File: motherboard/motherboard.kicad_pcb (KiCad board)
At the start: 2 copper layers, 33 parts, among them J1 Conn_01x02_Male, J2 Conn_01x02_Male, J3 Conn_01x02_Male, J4 Conn_01x02_Male, J5 XLR3, J6 Conn_01x02_Male, P1 Raspberry_Pi_+_Conn, Q1 Q_NMOS_GSD, Q2 Q_NMOS_GSD, U1 74AUC2G04, U2 4081, U3 TLC272, U4 TLC272

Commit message: First routing done!
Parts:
- removed C2: C, Capacitor_SMD:C_0603_1608Metric
- removed D4, D5: D, Diode_SMD:D_0603_1608Metric
- removed R12: 4.7k, Resistor_SMD:R_0201_0603Metric
- removed RV2: 10k, Potentiometer_SMD:Potentiometer_Vishay_TS53YL_Vertical
- removed U4: TLC272, Package_SO:TSSOP-8_4.4x3mm_P0.65mm
- added D1: d, Diode_SMD:D_0603_1608Metric, F.Cu at (115.4, 64.9)
- added G***: LOGO, silkscreen:logo_2, F.Cu at (103.1, 95.8)
- D2, D3: value d -> D
- J5: value XLR3 -> Conn_01x02_Male; footprint TerminalBlock_Phoenix:TerminalBlock_Phoenix_MKDS-3-3-5.08_1x03_P5.08mm_Horizontal -> TerminalBlock_Phoenix:TerminalBlock_Phoenix_MKDS-1,5-2-5.08_1x02_P5.08mm_Horizontal
- J6: value Conn_01x02_Male -> XLR3; footprint TerminalBlock_Phoenix:TerminalBlock_Phoenix_MKDS-1,5-2-5.08_1x02_P5.08mm_Horizontal -> TerminalBlock_Phoenix:TerminalBlock_Phoenix_MKDS-3-3-5.08_1x03_P5.08mm_Horizontal
- R1, R10, R2, R3, R8: footprint Resistor_SMD:R_0201_0603Metric -> Resistor_SMD:R_0603_1608Metric_Pad1.05x0.95mm_HandSolder
- R11: value 100 -> 4.7k; footprint Resistor_SMD:R_0201_0603Metric -> Resistor_SMD:R_0603_1608Metric_Pad1.05x0.95mm_HandSolder
- R4: value 230 -> 100k; footprint Resistor_SMD:R_0201_0603Metric -> Resistor_SMD:R_0603_1608Metric_Pad1.05x0.95mm_HandSolder
- R5: value 230 -> 30; footprint Resistor_SMD:R_0201_0603Metric -> Resistor_SMD:R_0603_1608Metric_Pad1.05x0.95mm_HandSolder
- R6: value 100k -> 230; footprint Resistor_SMD:R_0201_0603Metric -> Resistor_SMD:R_0603_1608Metric_Pad1.05x0.95mm_HandSolder
- R7: value 30 -> 230; footprint Resistor_SMD:R_0201_0603Metric -> Resistor_SMD:R_0603_1608Metric_Pad1.05x0.95mm_HandSolder
- R9: value 230 -> 100; footprint Resistor_SMD:R_0201_0603Metric -> Resistor_SMD:R_0603_1608Metric_Pad1.05x0.95mm_HandSolder
- moved J6 99.4 mm to (52.8, 106.5), turned to 180 degrees
- moved R9 94.2 mm to (48.4, 87.9), turned to 90 degrees
- moved D2 83.6 mm to (44.5, 92.8), turned to 270 degrees
- moved J5 80.5 mm to (131.2, 80.7), turned to 90 degrees
- moved D3 70.1 mm to (53.1, 89.6)
- moved U2 44.3 mm to (96.1, 36.0)
- moved U1 43.7 mm to (88.2, 34.3)
- moved J2 35.3 mm to (131.3, 51.2), turned to 90 degrees
- moved R1 35.1 mm to (123.5, 45.9), turned to 180 degrees
- moved J3 22.2 mm to (131.3, 37.2)
- moved R5 21.9 mm to (118.1, 43.5), turned to 270 degrees
- moved R6 21.5 mm to (116.3, 61.0), turned to 180 degrees
- moved J4 17.6 mm to (131.3, 65.0)
- moved U3 17.6 mm to (114.9, 49.5)
- moved RV1 13.6 mm to (111.3, 58.1), turned to 270 degrees
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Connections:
- D2 pad 1: GND -> Net-(D2-Pad1)
- D2 pad 2: Net-(D2-Pad2) -> GND
- D3 pad 1: GND -> /Temp_interface/+3.3V
- D3 pad 2: Net-(D3-Pad2) -> Net-(D2-Pad1)
- J2 pad 2: /SSR_interface/SSR_driver_1/ssr_in -> Net-(J2-Pad2)
- J3 pad 2: Net-(J3-Pad2) -> /SSR_interface/SSR_driver_1/ssr_in
- J5 pad 1: /Temp_interface/+3.3V -> GND
- J6 pad 1: GND -> /Temp_interface/+3.3V
- Q1 pad 2: Net-(Q1-Pad2) -> /SSR_interface/SSR_driver_1/indicator
- Q2 pad 2: Net-(Q2-Pad2) -> /SSR_interface/SSR_driver_2/indicator
- R1 pad 1: Net-(J6-Pad2) -> Net-(J2-Pad2)
- R10 pad 1: Net-(D4-Pad1) -> Net-(J6-Pad2)
- R10 pad 2: /Temp_interface/TEMP_GPIO -> Net-(D2-Pad1)
- R11 pad 1: Net-(J5-Pad2) -> /Temp_interface/+3.3V
- R11 pad 2: Net-(D4-Pad1) -> Net-(J6-Pad2)
- R3 pad 1: Net-(Q1-Pad2) -> /SSR_interface/SSR_driver_1/indicator
- R4 pad 1: +5V -> /SSR_interface/SSR_driver_2/sig_in
- R4 pad 2: Net-(D2-Pad2) -> GND
- R5 pad 1: Net-(R5-Pad1) -> /SSR_interface/SSR_driver_2/indicator
- R5 pad 2: Net-(J3-Pad2) -> GND
- R6 pad 1: /SSR_interface/SSR_driver_2/sig_in -> +5V
- R6 pad 2: GND -> Net-(D1-Pad2)
- R7 pad 1: Net-(Q2-Pad2) -> Net-(R7-Pad1)
- R7 pad 2: GND -> Net-(J4-Pad2)
- R8 pad 1: +5V -> Net-(R8-Pad1)
- R8 pad 2: Net-(D3-Pad2) -> Net-(J5-Pad2)
- R9 pad 1: Net-(R9-Pad1) -> Net-(D2-Pad1)
- R9 pad 2: Net-(J4-Pad2) -> /Temp_interface/TEMP_GPIO
- RV1 pad 1: Net-(D2-Pad2) -> Net-(D1-Pad2)
- U3 pad 1: Net-(R5-Pad1) -> Net-(R7-Pad1)
- U3 pad 3: Net-(Q1-Pad2) -> /SSR_interface/SSR_driver_2/indicator
- U3 pad 5: Net-(U3-Pad5) -> /SSR_interface/SSR_driver_1/indicator
- U3 pad 6: Net-(U3-Pad6) -> Net-(C1-Pad1)
- U3 pad 7: Net-(U3-Pad7) -> Net-(R8-Pad1)
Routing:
- net +5V: track 0.00 -> 104.3 mm, vias 0 -> 4
- net /Temp_interface/+3.3V: track 0.00 -> 66.2 mm
- net /SSR_interface/SSR2_GPIO: track 0.00 -> 63.2 mm
- net /Temp_interface/TEMP_GPIO: track 0.00 -> 60.3 mm
- net /SSR_interface/SSR1_GPIO: track 0.00 -> 57.5 mm
- net Net-(R1-Pad2): track 0.00 -> 29.2 mm, vias 0 -> 2
- net /SSR_interface/SSR_driver_2/sig_in: track 0.00 -> 29.0 mm, vias 0 -> 2
- net GND: track 0.00 -> 24.7 mm, vias 0 -> 3
- net Net-(J5-Pad2): track 0.00 -> 24.5 mm
- net /SSR_interface/SSR_driver_1/sig_in: track 0.00 -> 21.6 mm, vias 0 -> 2
- net /SSR_interface/SSR_driver_1/ssr_in: track 0.00 -> 21.5 mm
- net Net-(C1-Pad1): track 0.00 -> 17.8 mm
- net /SSR_interface/SSR_driver_2/indicator: track 0.00 -> 14.0 mm
- net Net-(J6-Pad2): track 0.00 -> 13.8 mm
- net Net-(J4-Pad2): track 0.00 -> 13.1 mm
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- added copper zone on B.Cu, net GND
- added copper zone on F.Cu, net GND

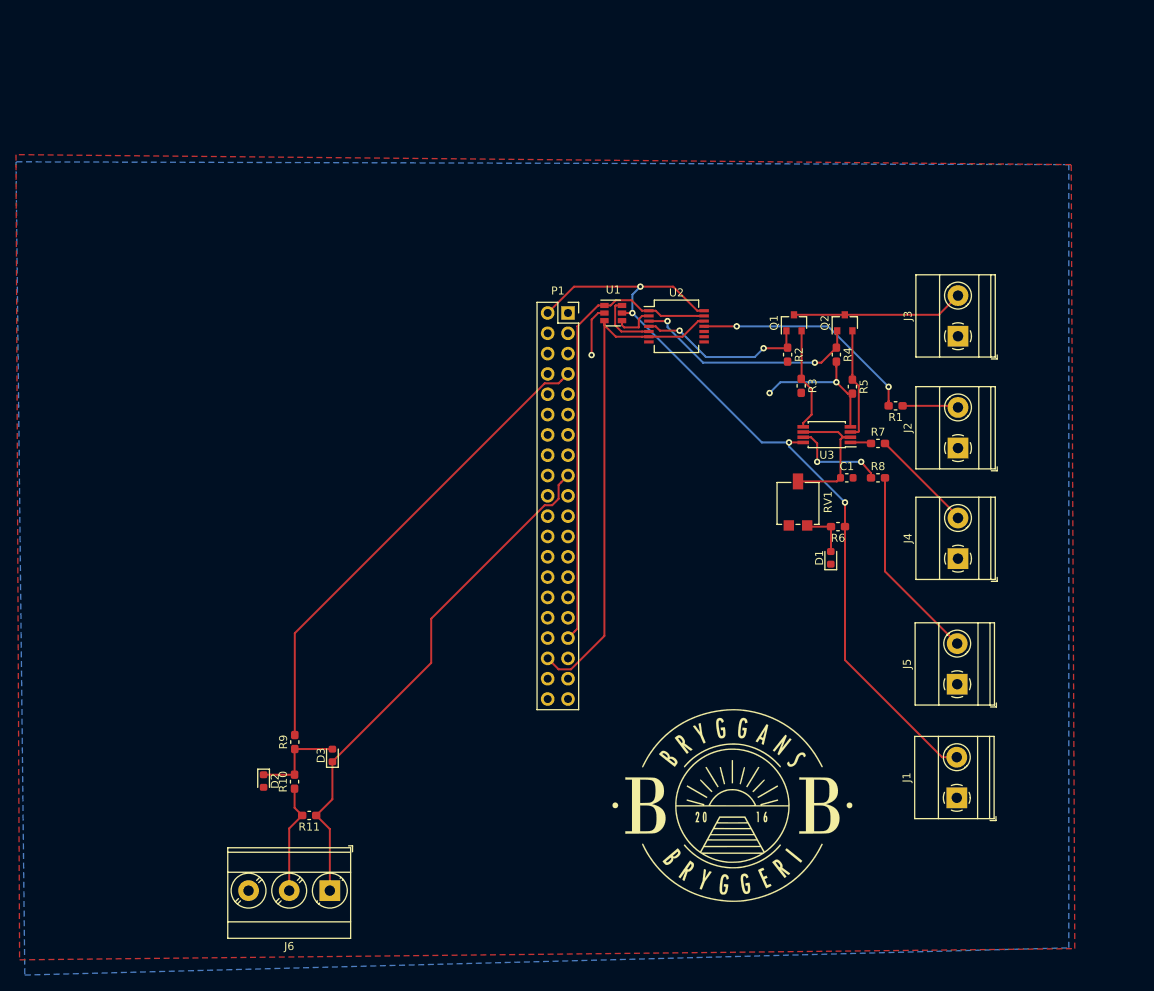
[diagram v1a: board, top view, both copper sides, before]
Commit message: Moved parts around
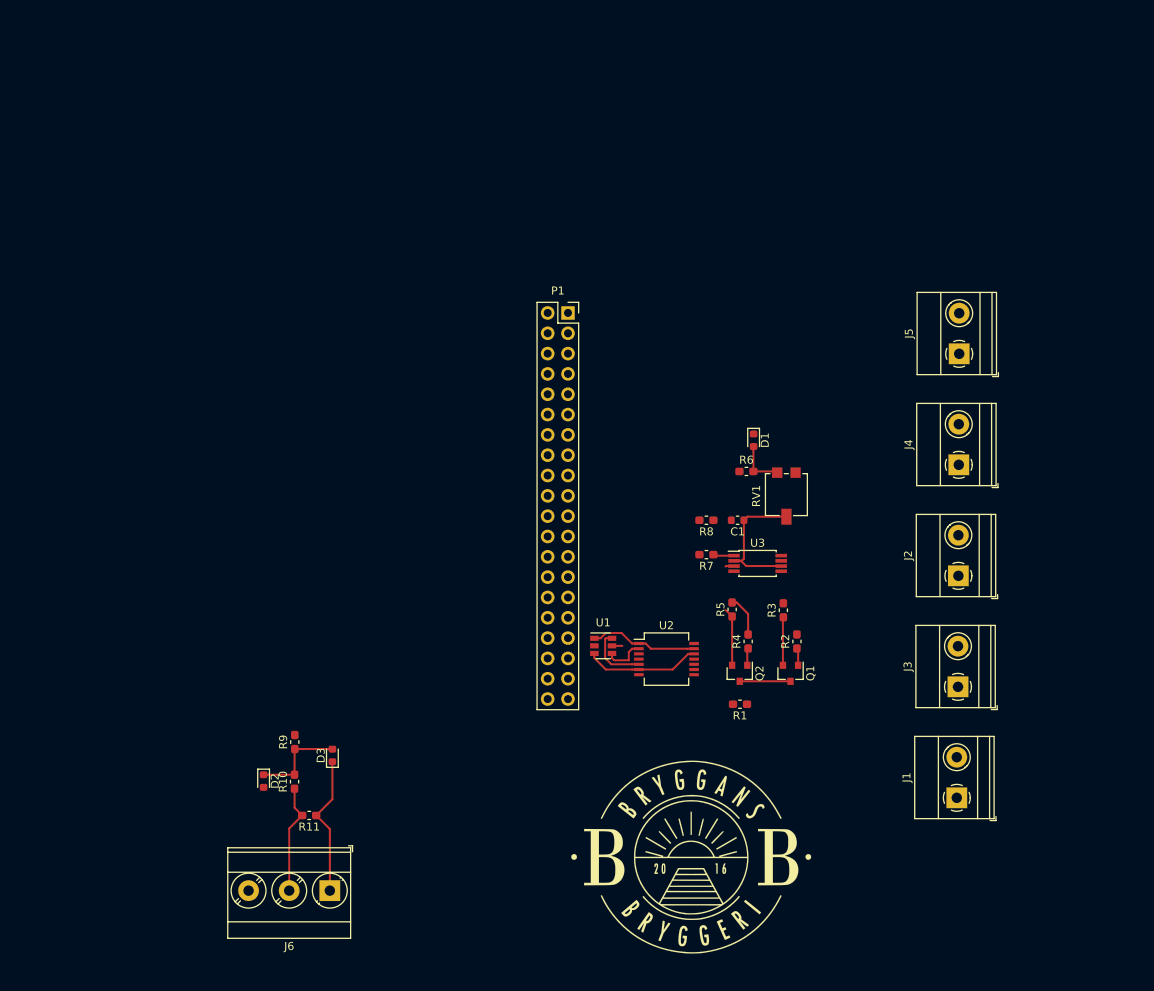
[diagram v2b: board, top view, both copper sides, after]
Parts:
- moved Q2 45.7 mm to (104.0, 79.3), turned to 270 degrees
- moved J3 43.8 mm to (131.3, 81.0)
- moved Q1 43.8 mm to (110.4, 79.3), turned to 270 degrees
- moved R1 42.1 mm to (104.0, 83.2)
- moved U1 41.6 mm to (87.0, 75.9)
- moved U2 41.6 mm to (94.9, 77.6)
- moved J5 41.3 mm to (131.4, 39.4)
- moved R4 37.5 mm to (105.1, 75.4), turned to 90 degrees
- moved R2 35.9 mm to (111.2, 75.4), turned to 90 degrees
- moved R5 31.7 mm to (103.1, 71.4), turned to 90 degrees
- moved R3 28.1 mm to (109.5, 71.5), turned to 90 degrees
- moved R7 25.6 mm to (99.8, 64.5), turned to 180 degrees
- moved R8 22.1 mm to (99.8, 60.2), turned to 180 degrees
- moved U3 18.3 mm to (106.2, 65.6), turned to 0 degrees
- moved D1 17.6 mm to (105.8, 50.2), turned to 270 degrees
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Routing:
- net +5V: track 104.3 -> 1.30 mm, vias 4 -> 0
- net /Temp_interface/TEMP_GPIO: track 60.3 -> 0.00 mm
- net /SSR_interface/SSR2_GPIO: track 63.2 -> 14.4 mm
- net /Temp_interface/+3.3V: track 66.2 -> 17.7 mm
- net /SSR_interface/SSR1_GPIO: track 57.5 -> 13.5 mm
- net Net-(R1-Pad2): track 29.2 -> 0.00 mm, vias 2 -> 0
- net /SSR_interface/SSR_driver_2/sig_in: track 29.0 -> 2.15 mm, vias 2 -> 0
- net Net-(J5-Pad2): track 24.5 -> 0.00 mm
- net GND: track 24.7 -> 5.17 mm, vias 3 -> 0
- net /SSR_interface/SSR_driver_1/sig_in: track 21.6 -> 2.17 mm, vias 2 -> 0
- net /SSR_interface/SSR_driver_1/ssr_in: track 21.5 -> 6.35 mm
- net Net-(J4-Pad2): track 13.1 -> 0.00 mm
- net Net-(R8-Pad1): track 12.3 -> 0.00 mm, vias 2 -> 0
- net Net-(J2-Pad2): track 7.01 -> 0.00 mm
- net /SSR_interface/SSR_driver_1/indicator: track 13.0 -> 6.03 mm
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- removed copper zone on B.Cu, net GND
- removed copper zone on F.Cu, net GND

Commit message: Ready for print?
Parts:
- moved P1 48.9 mm to (75.3, 82.7), turned to 180 degrees
- moved J3 44.2 mm to (116.3, 39.4)
- moved Q1 37.4 mm to (100.1, 43.4)
- moved R2 37.4 mm to (100.9, 39.4)
- moved R3 37.4 mm to (99.2, 35.5)
- moved Q2 36.0 mm to (105.7, 43.4)
- moved R4 36.0 mm to (106.7, 39.4)
- moved R5 36.0 mm to (104.7, 35.4)
- moved R1 35.3 mm to (99.2, 48.2)
- moved U1 35.1 mm to (83.3, 40.9)
- moved U2 35.1 mm to (91.2, 42.6)
- moved D2 34.5 mm to (70.7, 70.4), turned to 90 degrees
- moved J5 30.9 mm to (116.2, 66.3)
- moved J4 30.5 mm to (116.1, 79.7)
- moved R9 26.5 mm to (71.5, 75.1), turned to 0 degrees
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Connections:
- P1 pad 1: Net-(P1-Pad1) -> /Temp_interface/+3.3V
- P1 pad 17: /Temp_interface/+3.3V -> Net-(P1-Pad17)
- P1 pad 33: /SSR_interface/SSR1_GPIO -> /SSR_interface/SSR2_GPIO
- P1 pad 36: /SSR_interface/SSR2_GPIO -> /SSR_interface/SSR1_GPIO
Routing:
- net +5V: track 1.30 -> 130.1 mm, vias 0 -> 3
- net /SSR_interface/SSR_driver_2/sig_in: track 2.15 -> 24.7 mm, vias 0 -> 2
- net Net-(J4-Pad2): track 0.00 -> 21.6 mm
- net Net-(J2-Pad2): track 0.00 -> 16.4 mm
- net /SSR_interface/SSR_driver_2/indicator: track 8.32 -> 23.8 mm, vias 0 -> 2
- net /SSR_interface/SSR_driver_1/ssr_in: track 6.35 -> 21.7 mm
- net /SSR_interface/SSR_driver_1/indicator: track 6.03 -> 20.7 mm, vias 0 -> 2
- net /SSR_interface/SSR_driver_1/sig_in: track 2.17 -> 16.2 mm, vias 0 -> 2
- net Net-(J5-Pad2): track 0.00 -> 12.4 mm
- net Net-(J6-Pad2): track 13.8 -> 25.5 mm
- net GND: track 5.17 -> 15.6 mm
- net Net-(R8-Pad1): track 0.00 -> 10.1 mm, vias 0 -> 2
- net /SSR_interface/SSR2_GPIO: track 14.4 -> 22.5 mm
- net Net-(R1-Pad2): track 0.00 -> 7.59 mm
- net /Temp_interface/+3.3V: track 17.7 -> 23.6 mm
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- added copper zone on F.Cu, net GND
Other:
- board text added: "BRYGGKORT v1.0"

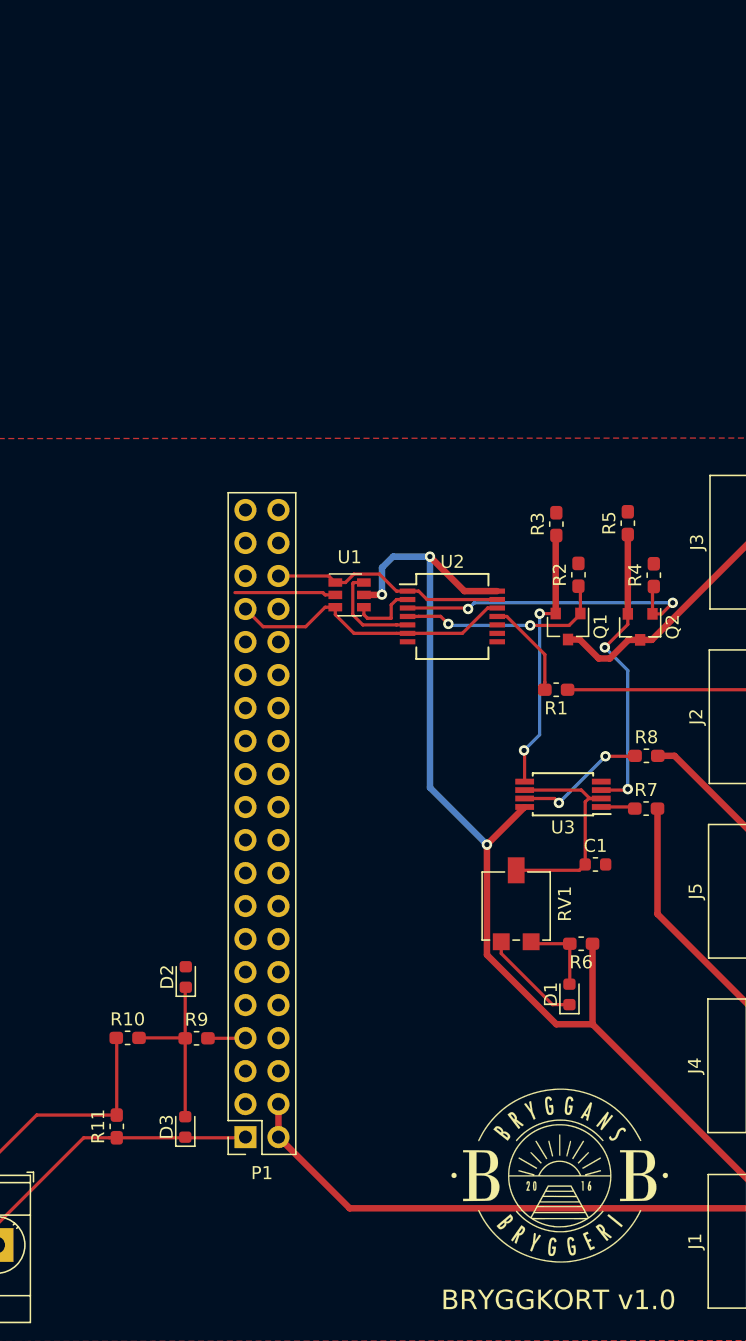
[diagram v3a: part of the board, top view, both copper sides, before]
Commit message: Added second SSR connector
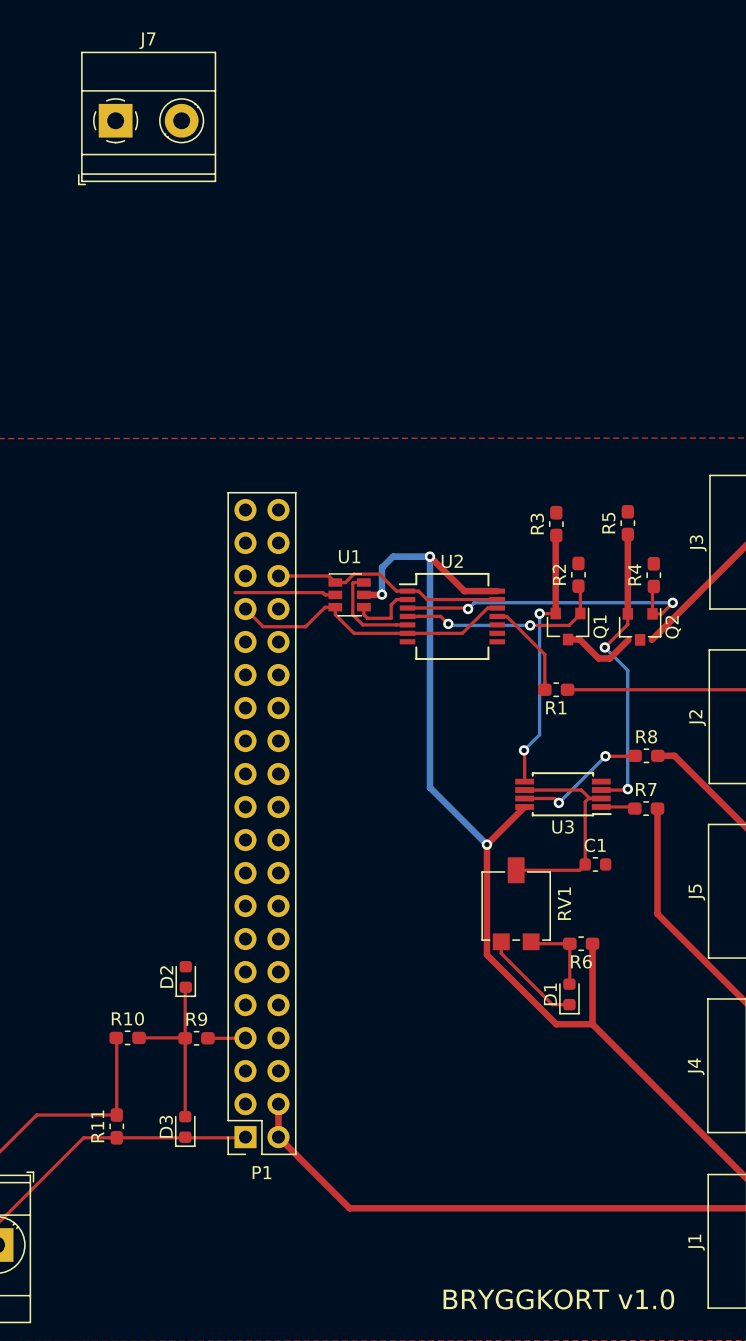
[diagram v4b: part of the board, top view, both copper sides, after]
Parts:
- removed G***: LOGO, silkscreen:logo_2
- added J7: Conn_01x02_Male, TerminalBlock_Phoenix:TerminalBlock_Phoenix_MKDS-1,5-2-5.08_1x02_P5.08mm_Horizontal, F.Cu at (65.3, 4.47)
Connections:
- P1 pad 10: Net-(P1-Pad10) -> (no net)
- P1 pad 11: Net-(P1-Pad11) -> (no net)
- P1 pad 12: Net-(P1-Pad12) -> (no net)
- P1 pad 13: Net-(P1-Pad13) -> (no net)
- P1 pad 14: Net-(P1-Pad14) -> (no net)
- P1 pad 15: Net-(P1-Pad15) -> (no net)
- P1 pad 16: Net-(P1-Pad16) -> (no net)
- P1 pad 17: Net-(P1-Pad17) -> (no net)
- P1 pad 18: Net-(P1-Pad18) -> (no net)
- P1 pad 19: Net-(P1-Pad19) -> (no net)
- P1 pad 21: Net-(P1-Pad21) -> (no net)
- P1 pad 22: Net-(P1-Pad22) -> (no net)
- P1 pad 23: Net-(P1-Pad23) -> (no net)
- P1 pad 24: Net-(P1-Pad24) -> (no net)
- P1 pad 25: Net-(P1-Pad25) -> (no net)
- P1 pad 26: Net-(P1-Pad26) -> (no net)
- P1 pad 27: Net-(P1-Pad27) -> (no net)
- P1 pad 28: Net-(P1-Pad28) -> (no net)
- P1 pad 29: Net-(P1-Pad29) -> (no net)
- P1 pad 3: Net-(P1-Pad3) -> (no net)
- P1 pad 30: Net-(P1-Pad30) -> (no net)
- P1 pad 31: Net-(P1-Pad31) -> (no net)
- P1 pad 32: Net-(P1-Pad32) -> (no net)
- P1 pad 34: Net-(P1-Pad34) -> (no net)
- P1 pad 35: Net-(P1-Pad35) -> (no net)
- P1 pad 37: Net-(P1-Pad37) -> (no net)
- P1 pad 38: Net-(P1-Pad38) -> (no net)
- P1 pad 39: Net-(P1-Pad39) -> (no net)
- P1 pad 40: Net-(P1-Pad40) -> (no net)
- P1 pad 5: Net-(P1-Pad5) -> (no net)
- P1 pad 6: Net-(P1-Pad6) -> (no net)
- P1 pad 8: Net-(P1-Pad8) -> (no net)
- P1 pad 9: Net-(P1-Pad9) -> (no net)
- Q2 pad 3: /SSR_interface/SSR_driver_1/ssr_in -> /SSR_interface/SSR_driver_2/ssr_in
- U2 pad 10: Net-(U2-Pad10) -> (no net)
- U2 pad 8: Net-(U2-Pad8) -> (no net)
- U2 pad 9: Net-(U2-Pad9) -> (no net)
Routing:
- net /SSR_interface/SSR_driver_1/ssr_in: track 21.7 -> 19.9 mm
